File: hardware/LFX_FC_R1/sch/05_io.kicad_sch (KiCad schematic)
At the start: 27 parts, among them J1 SM08B-SRSS-TB, J5 SM04B-SRSS-TB, J6 SM02B-SRSS-TB, Q1 AO3400A, U6 TPD4E05U06DQA

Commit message: hardware: LFX_FC_R1 46x46 layout routed, DRC + parity clean
- 46 x 46 mm, M3 NPTH holes in the corners (39 x 39 mm pattern),
  JST-SH connectors on the edges, ESC S/G solder pads at the four corners
- IMU turned 90 deg so CS/SCK/MOSI/MISO face module pins 6..9 in order;
  the four lines are drawn (route_critical.hand_route_imu), not searched
- via/track keep-outs under the IMU and barometer bodies, 0.5 mm routing
  keep-out round the board rim
- EN divider re-laid as one column (U1.3 -> R1 -> R2 -> D2)
- VBAT divider top resistor moved to the battery end; only the divided
  node crosses the board
- GPS ESD at J5, series resistors at the module pins, no crossings
- router: hole-to-hole on same-net vias, 5 um freerouting clearance margin,
  off-plane fan-out vias removed
- schematic parity: global labels, library nicknames, MountingPin
  connectors, #FLG power flags, BOM exclusion for bare pads
- ERC 0, DRC 0 violations / 0 unconnected / 0 footprint errors
  (--schematic-parity)

Co-Authored-By: Claude Opus 5.5 <noreply@anthropic.com>
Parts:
- added J10: M4 pad, LFX:SolderPad_1.5x2.5mm, symbol Connector:TestPoint
- added J11: M1 GND, LFX:SolderPad_1.5x2.5mm, symbol Connector:TestPoint
- added J12: M2 GND, LFX:SolderPad_1.5x2.5mm, symbol Connector:TestPoint
- added J13: M3 GND, LFX:SolderPad_1.5x2.5mm, symbol Connector:TestPoint
- added J14: M4 GND, LFX:SolderPad_1.5x2.5mm, symbol Connector:TestPoint
- added J7: M1 pad, LFX:SolderPad_1.5x2.5mm, symbol Connector:TestPoint
- added J8: M2 pad, LFX:SolderPad_1.5x2.5mm, symbol Connector:TestPoint
- added J9: M3 pad, LFX:SolderPad_1.5x2.5mm, symbol Connector:TestPoint
- H1, H2, H3, H4: footprint (none) -> MountingHole:MountingHole_3.2mm_M3; now left out of the parts list
- J1: symbol Connector:Conn_01x08_Pin -> Connector_Generic_MountingPin:Conn_01x08_MountingPin
- J5: symbol Connector:Conn_01x04_Pin -> Connector_Generic_MountingPin:Conn_01x04_MountingPin
- J6: symbol Connector:Conn_01x02_Pin -> Connector_Generic_MountingPin:Conn_01x02_MountingPin
- TP4: now left out of the parts list
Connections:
- net ESC_M1: now also J7.1
- net ESC_M2: now also J8.1
- net ESC_M3: now also J9.1
- net ESC_M4: now also J10.1
- net GND: now also J1.MP (MountPin), J5.MP (MountPin), J6.MP (MountPin), J11.1, J12.1, J13.1, J14.1
- net DBG_RX_X: no longer names the net of U6.5 (D2-)
- net DBG_TX_X: no longer names the net of U6.4 (D2+)
- no-connect marks 4 -> 6
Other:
- note added: "Separate ESC solder pads (quad-X corners)"
- moved on the sheet: D7, Q1, R12, R13, R14, R15, R20, R21, R22, R23, TP4, U6

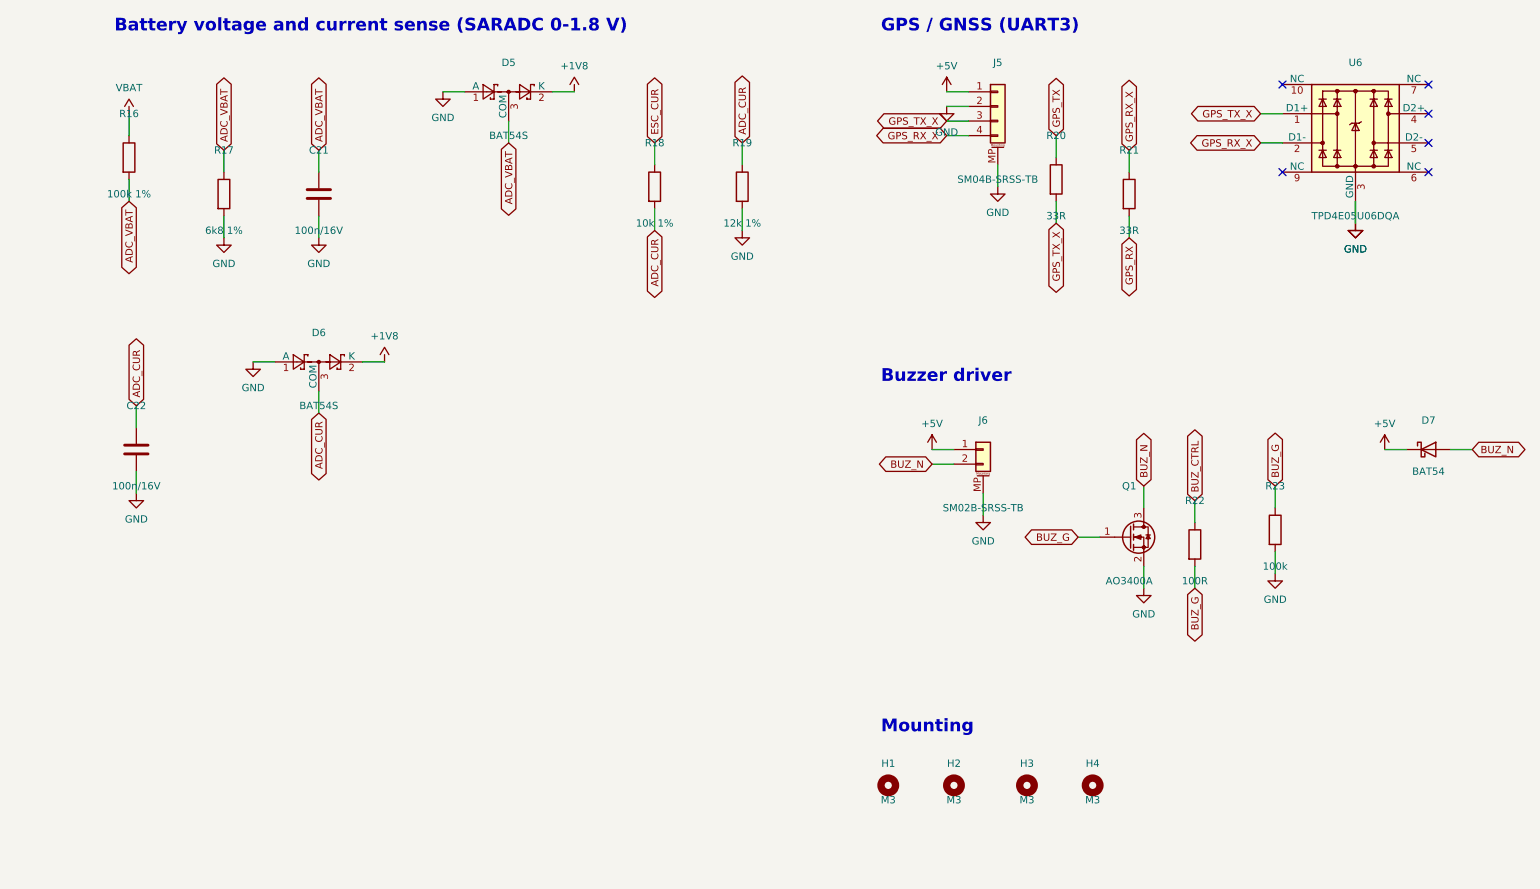
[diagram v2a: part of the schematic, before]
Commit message: hardware: LFX_LTE_R1 stacked LTE + GNSS board, FC link on J5
New 46 x 46 mm board hardware/LFX_LTE_R1 (same 39 mm M3 pattern, stacks on
the flight controller, all parts on the top side):
- Lierda NT26-KCN E LTE Cat.1 bis + GNSS (order the GPS + BDS variant);
  symbol and LCC/LGA-109 land pattern drawn from the Lierda hardware design
  manual Rev1.0 (table 2-5, fig. 2-2, fig. 8-3)
- TLV62569 buck +5V -> 3.8 V (modem VBAT 3.3-4.5 V), In2 +3V8 plane,
  2 x 47 uF + 100n / 33p / 8p2 at VBAT; TLV75533 3.3 V for the translators
- UART 3.3 <-> 1.8 V by 2 x SN74LVC1T45 (Hi-Z while the modem is off)
- Luckfox reflashes the modem: RESET_N via AO3400A, USB_BOOT via 1k from the
  1.8 V BOOT pin; USB / debug test pads for a PC rescue
- hinged nano-SIM with 22R / 33p / TPD4E05U06, LTE and GNSS U.FL with pi
  match, 50 ohm 0.35 mm feeds, active GNSS antenna bias
- ERC 0, DRC 0 violations / 0 unconnected / 0 parity

LFX_FC_R1 stays 46 x 46 mm:
- J5 GPS (JST-SH 4) -> LTE board link (JST-SH 10): 5V x2, GND x2, UART3,
  RESET (pin 18), BOOT (pin 20), buzzer gate, ESC current
- buzzer gate and ESC current now come from the modem's GPIO1 / ADC0
- ERC 0, DRC 0 violations / 0 unconnected / 0 parity

Shared: NT26-KCN and SIM_Card_Shield in the LFX library, stacked symbol
pins in gen_sch, route_pcb creates pcb/.  README and architecture docs
updated.

Co-Authored-By: Claude Opus 5.5 <noreply@anthropic.com>
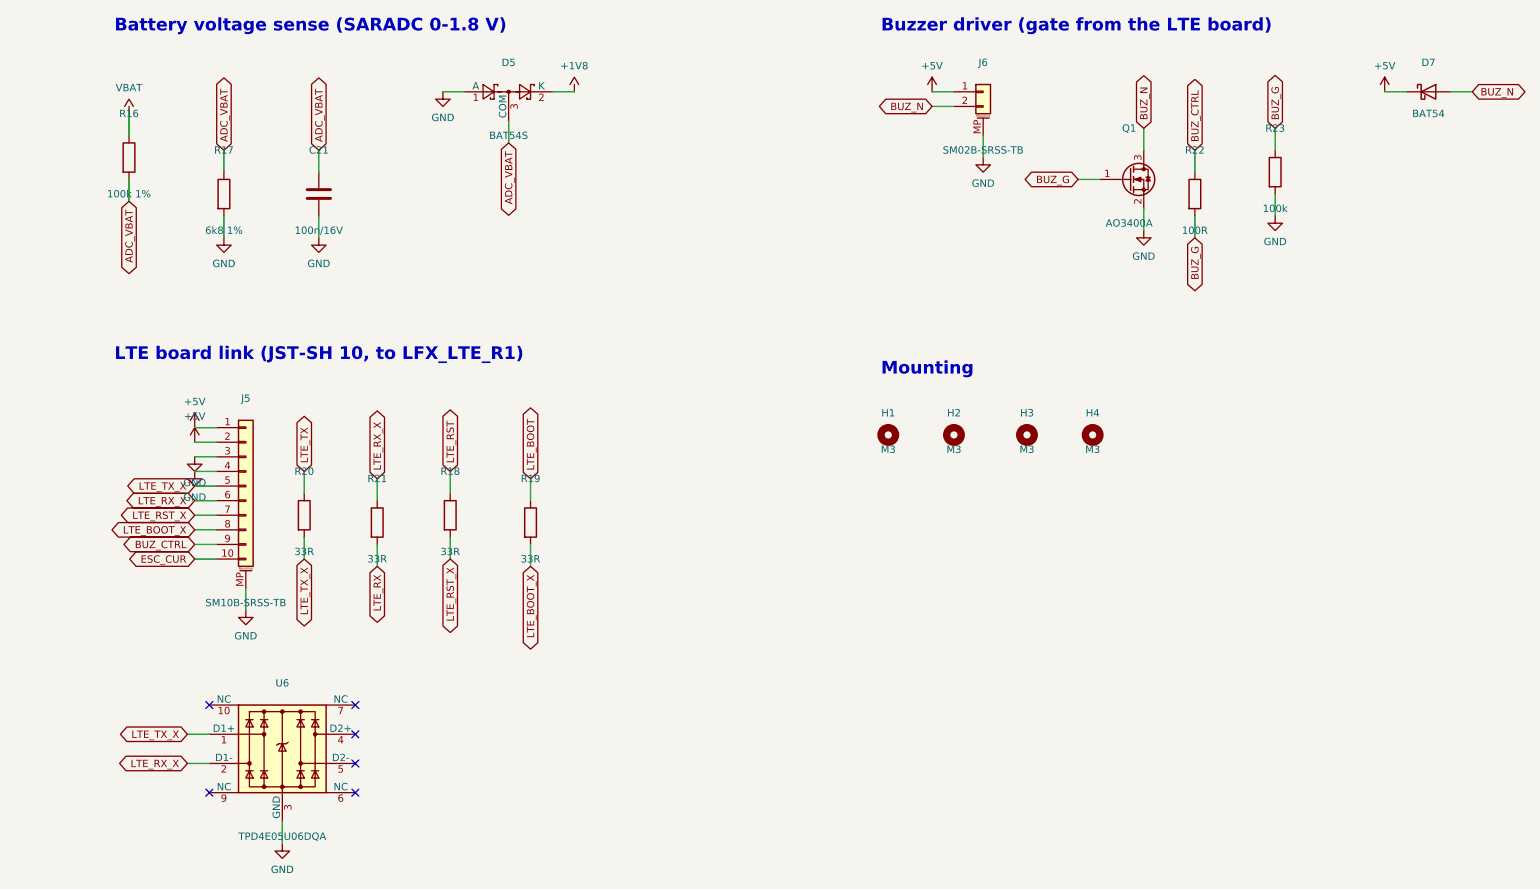
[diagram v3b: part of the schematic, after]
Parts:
- removed C22: 100n/16V, Capacitor_SMD:C_0402_1005Metric, symbol Device:C
- removed D6: BAT54S, Package_TO_SOT_SMD:SOT-23, symbol Diode:BAT54S
- J5: value SM04B-SRSS-TB -> SM10B-SRSS-TB; footprint Connector_JST:JST_SH_SM04B-SRSS-TB_1x04-1MP_P1.00mm_Horizontal -> Connector_JST:JST_SH_SM10B-SRSS-TB_1x10-1MP_P1.00mm_Horizontal; symbol Connector_Generic_MountingPin:Conn_01x04_MountingPin -> Connector_Generic_MountingPin:Conn_01x10_MountingPin
- R18: value 10k 1% -> 33R; footprint Resistor_SMD:R_0603_1608Metric -> Resistor_SMD:R_0402_1005Metric
- R19: value 12k 1% -> 33R; footprint Resistor_SMD:R_0603_1608Metric -> Resistor_SMD:R_0402_1005Metric
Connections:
- net +5V: now also J5.2 (Pin_2)
- net BUZ_CTRL: now also J5.9 (Pin_9)
- net ESC_CUR: now also J5.10 (Pin_10); no longer R18.1
- net GND: now also J5.3 (Pin_3), J5.4 (Pin_4); no longer J5.2 (Pin_2), R19.2
- net ADC_CUR renamed LTE_BOOT
- net LTE_BOOT: no longer R18.2
- net GPS_RX renamed LTE_RX
- net GPS_RX_X renamed LTE_RX_X
- net LTE_RX_X: now also J5.6 (Pin_6); no longer J5.4 (Pin_4)
- net GPS_TX renamed LTE_TX
- net GPS_TX_X renamed LTE_TX_X
- net LTE_TX_X: now also J5.5 (Pin_5); no longer J5.3 (Pin_3)
- new net LTE_BOOT_X: J5.8 (Pin_8), R19.2
- new net LTE_RST: R18.1
- new net LTE_RST_X: J5.7 (Pin_7), R18.2
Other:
- note added: "Battery voltage sense (SARADC 0-1.8 V)"
- note added: "Buzzer driver (gate from the LTE board)"
- note added: "LTE board link (JST-SH 10, to LFX_LTE_R1)"
- note removed: "Battery voltage and current sense (SARADC 0-1.8 V)"
- note removed: "Buzzer driver"
- note removed: "GPS / GNSS (UART3)"
- moved on the sheet: D7, H1, H2, H3, H4, J6, Q1, R18, R19, R20, R21, R22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
